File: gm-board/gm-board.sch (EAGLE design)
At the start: 43 parts, among them IC1 ZXCT1109, J1 SWD_SHROUD, J2 HV_GEN

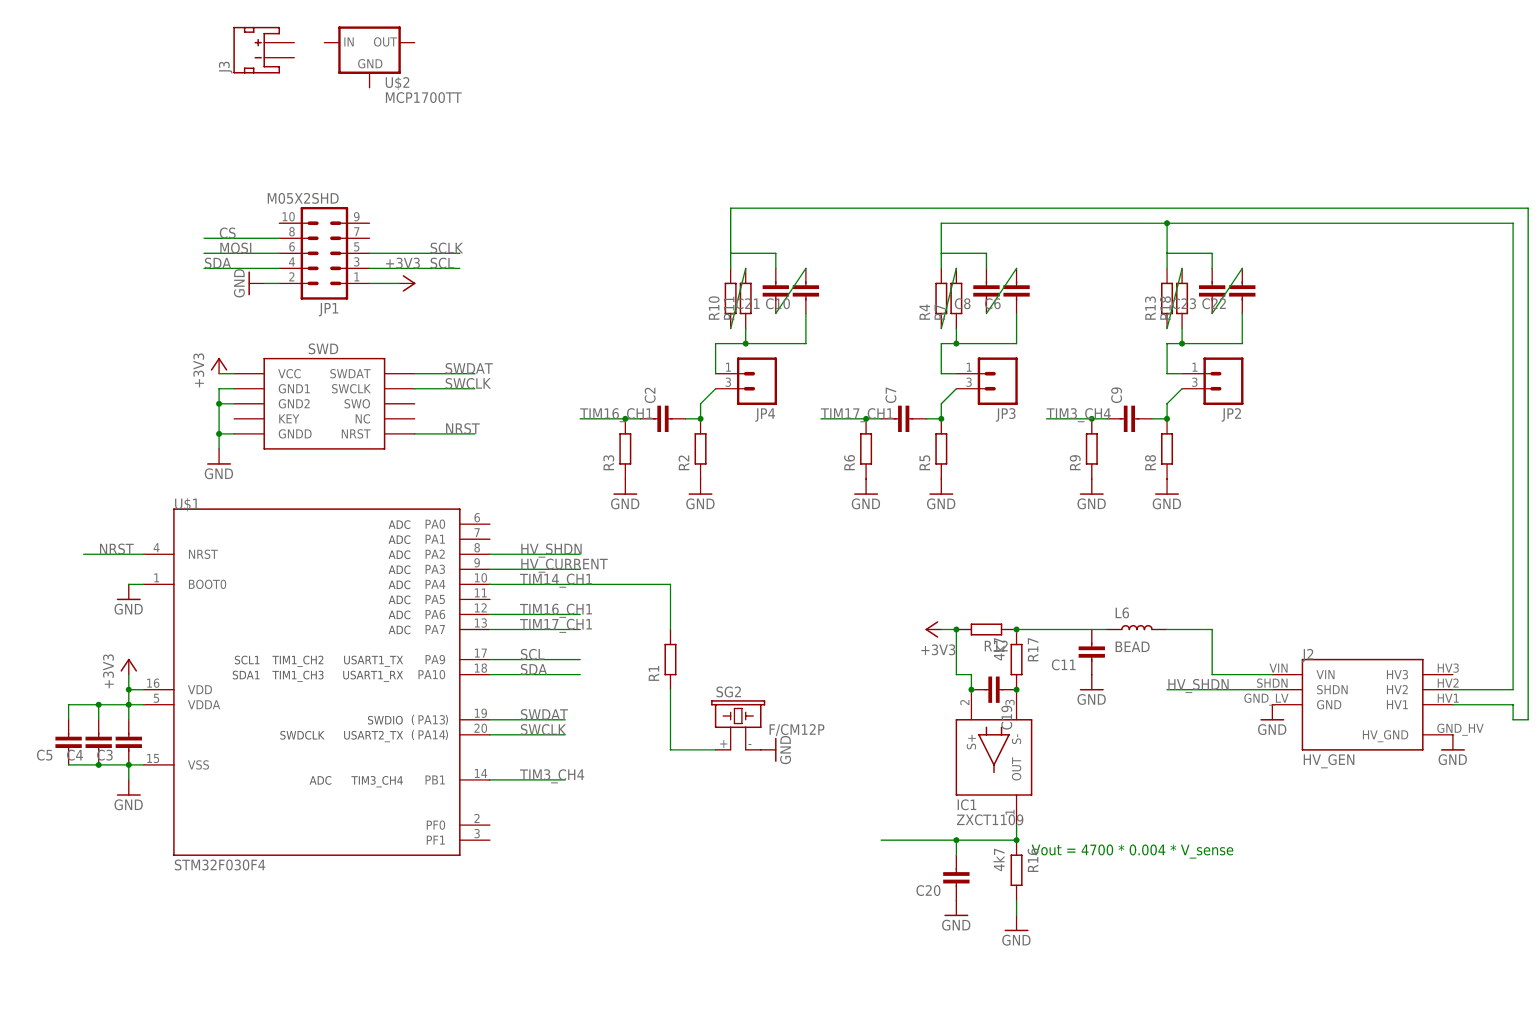
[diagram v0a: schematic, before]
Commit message: adding part ordering numbers
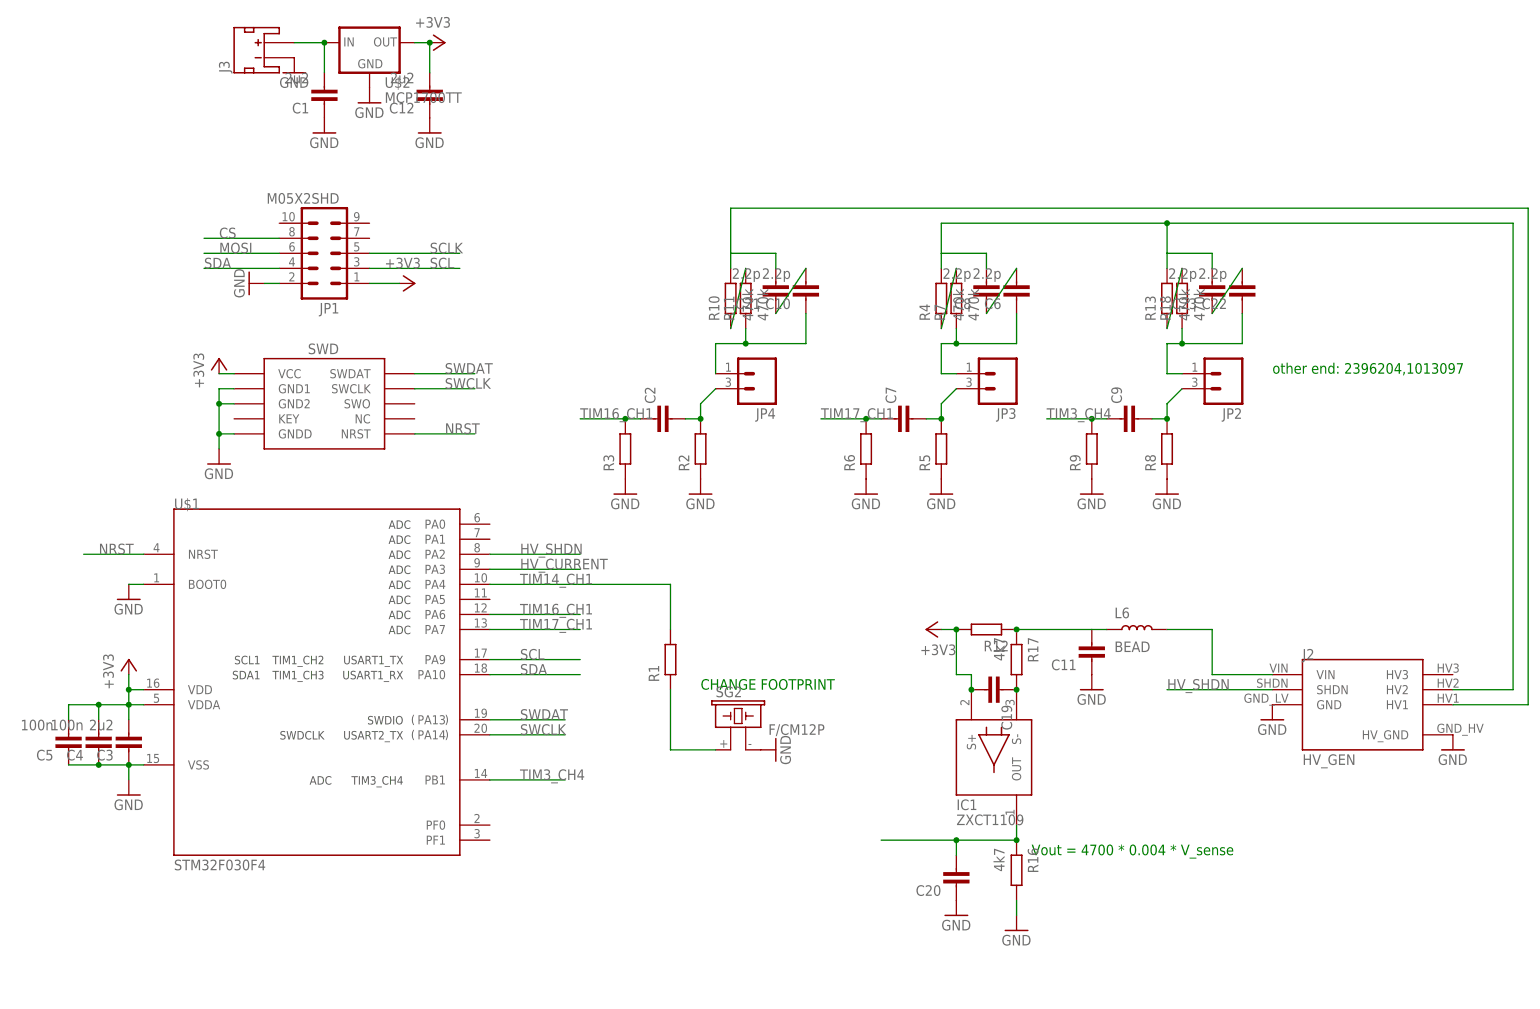
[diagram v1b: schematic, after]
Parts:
- added C1, C12: 2u2, passives-7351:CAPACITOR0603-N
- C10, C21, C22, C23, C6, C8: value (none) -> 2.2p; FARNELL (none) -> 1855767
- C3: value (none) -> 2u2; FARNELL (none) -> 2496923
- C4, C5: value (none) -> 100n
- IC1: FARNELL (none) -> 1904028
- JP2, JP3, JP4: FARNELL (none) -> 1462950
- L6: FARNELL (none) -> 1781093
- R10, R13, R18, R4, R7: value (none) -> 470k; FARNELL (none) -> 1576201
- R11: value (none) -> 470k
- R12: FARNELL (none) -> 2328089
- SG2: FARNELL (none) -> 1823866
- U$1: FARNELL (none) -> 2393635
- U$2: FANRELL (none) -> 1296592
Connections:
- new net N$10: C1.2, J3.+, U$2.IN
- net +3V3: now also C12.2, U$2.OUT
- net GND: now also C1.1, C12.1, J3.-, U$2.GND
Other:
- note added: "CHANGE FOOTPRINT"
- note added: "other end: 2396204,1013097"

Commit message: almost done
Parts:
- removed C19: (no value), passives-7351:CAPACITOR0603-N
- removed C22, C23: 2.2p, passives-7351:CAPACITOR0805-N
- removed R17: 4k7, passives-7351:RESISTOR0603-N
- removed R18: 470k, passives-7351:RESISTOR1206-N
- removed SG2: F/CM12P, buzzer:F/CM12P
- removed U$2: MCP1700TT, dtb:MCP1700TT
- added C13: (no value), passives-7351:CAPACITOR0603-N
- added C16: 2.2p, passives-7351:CAPACITOR0805-N
- added C17: 100n, passives-7351:CAPACITOR0603-N
- added IC2: ZXCT1109, dtb:ZXCT1109
- added R14, R15: 470k, passives-7351:RESISTOR1206-N
- added SJ1: JUMPER-PAD-3-2OF3_NC_BY_PASTE, SparkFun-Passives:JUMPER-PAD-3-2OF3_NC_BY_PASTE
- added X1: PKM13EPYH, Mine:PKM13EPYH
- C1, C12, C3: value 2u2 -> (none); FARNELL 2496923 -> (none)
- C11: value (none) -> 2.2p; device passives-7351:CAPACITOR0603-N -> passives-7351:CAPACITOR0805-N; FARNELL (none) -> 1855767
- C2, C9: value (none) -> 2u2; FARNELL (none) -> 2496923
- C4: value 100n -> 2u2; FARNELL (none) -> 2496923
- C5: value 100n -> 2.2p; device passives-7351:CAPACITOR0603-N -> passives-7351:CAPACITOR0805-N; FARNELL (none) -> 1855767
- C8: value 2.2p -> 100n; device passives-7351:CAPACITOR0805-N -> passives-7351:CAPACITOR0603-N; FARNELL 1855767 -> (none)
- IC1: value ZXCT1109 -> MCP1700TT; device dtb:ZXCT1109 -> dtb:MCP1700TT; FANRELL (none) -> 1296592; FARNELL 1904028 -> (none)
- J1: value SWD_SHROUD -> HV_GEN-HOLE; device dtb:SWD_SHROUD -> generator-lib:HV_GEN-HOLE
- J2: value HV_GEN -> (none); device generator-lib:HV_GEN -> dtb:JST_2MM_MALE_TH
- J3: value (none) -> SWD_SHROUD; device dtb:JST_2MM_MALE_TH -> dtb:SWD_SHROUD
- JP1: value M05X2SHD -> (none); device SparkFun-Connectors:M05X2SHD -> Mine:M02-HV; FARNELL (none) -> 1462950
- JP2: value (none) -> M05X2SHD; device Mine:M02-HV -> SparkFun-Connectors:M05X2SHD; FARNELL 1462950 -> (none)
- R1, R6: value (none) -> 4k7
- R11: value 470k -> (none); device passives-7351:RESISTOR1206-N -> passives-7351:RESISTOR0603-N
- R12: FARNELL 2328089 -> (none)
- R13, R7: value 470k -> (none); device passives-7351:RESISTOR1206-N -> passives-7351:RESISTOR0603-N; FARNELL 1576201 -> (none)
- R16: value 4k7 -> (none)
- R2: FARNELL (none) -> 2328089
- R3, R9: value (none) -> 470k; device passives-7351:RESISTOR0603-N -> passives-7351:RESISTOR1206-N; FARNELL (none) -> 1576201
- renumbered C20 to C14, C21 to C15, L6 to L1, U$1 to IC3
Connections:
- removed net N$10: C1.2, J3.+, U$2.IN
- new net N$11: C3.2, IC2.S+, R2.P$2, SJ1.2
- new net VIN: C4.2, IC1.IN, J2.+, SJ1.1
- net +3V3: now also C17.2, C2.2, C8.2, C9.2, IC1.OUT, J3.VCC, JP2.1, SJ1.3; no longer C12.2, C19.2, C3.2, C4.2, C5.2, IC1.S+, J1.VCC, JP1.1, R12.P$2, U$2.OUT
- net CS: now also JP2.8; no longer JP1.8
- net GND: now also C17.1, C2.1, C8.1, C9.1, IC1.GND, J1.GND, J1.HV_GND, J2.-, J3.GND1, J3.GND2, J3.GNDD, JP2.2, R11.P$1, R13.P$1, R16.P$1, R6.P$2, R7.P$1, X1.2; no longer C11.1, C12.1, C3.1, C5.1, J1.GND1, J1.GND2, J1.GNDD, J2.GND, J2.HV_GND, J3.-, JP1.2, R16.P$2, R2.P$1, R3.P$1, R6.P$1, R9.P$1, SG2.2, U$2.GND
- net HV_CURRENT: now also IC2.OUT, R6.P$1; no longer IC1.OUT, R16.P$1
- net HV_SHDN: now also J1.SHDN; no longer J2.SHDN
- net MOSI: now also JP2.6; no longer JP1.6
- net N$1: now also C13.2, R13.P$2; no longer C2.2, R2.P$2
- net N$16: now also C16.2; no longer C10.2
- net N$18: now also C3.1, IC2.S-, R1.P$2; no longer C19.1, IC1.S-, R17.P$2
- net N$19: now also C11.1, R10.P$1; no longer C6.1, R7.P$1
- net N$2: now also J1.VIN; no longer J2.VIN
- net N$20: now also C10.2, C5.2, J1.HV2, R3.P$2, R9.P$2; no longer C23.2, C8.2, J2.HV2, R13.P$2, R4.P$2
- net N$21: now also R10.P$2, R9.P$1; no longer R4.P$1, R7.P$2
- net N$22: now also C10.1, C11.2; no longer C6.2, C8.1
- net N$23: now also C6.1, JP1.1, R4.P$1; no longer C22.1, JP2.1, R18.P$1
- net N$25: now also R3.P$1, R4.P$2; no longer R13.P$1, R18.P$2
- net N$26: now also C5.1, C6.2; no longer C22.2, C23.1
- net N$3: now also C16.1, R15.P$1; no longer C10.1, R11.P$1
- net N$4: now also R14.P$1, R15.P$2; no longer R10.P$1, R11.P$2
- net N$5: now also C12.2, R11.P$2; no longer C7.2, R5.P$2
- net N$6: now also R12.P$1, X1.1; no longer R1.P$1, SG2.1
- net N$7: now also C1.2, R1.P$1, R2.P$1; no longer C11.2, R12.P$1, R17.P$1
- net N$8: now also J1.HV1, R14.P$2; no longer J2.HV1, R10.P$2
- net N$9: now also C7.2, JP1.2, R5.P$2; no longer C9.2, JP2.2, R8.P$2
- net NRST: now also J3.NRST; no longer J1.NRST
- net SCL: now also JP2.3; no longer JP1.3
- net SCLK: now also JP2.5; no longer JP1.5
- net SDA: now also JP2.4; no longer JP1.4
- net SWCLK: now also J3.SWCLK; no longer J1.SWCLK
- net SWDAT: now also J3.SWDAT; no longer J1.SWDAT
- net TIM14_CH1: now also R12.P$2; no longer R1.P$2
- net TIM16_CH1: now also C13.1, R16.P$2; no longer C2.1, R3.P$2
- net TIM17_CH1: now also C12.1, R8.P$2; no longer C7.1, R6.P$2
- net TIM3_CH4: now also C7.1, R7.P$2; no longer C9.1, R9.P$2
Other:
- note removed: "CHANGE FOOTPRINT"
- moved on the sheet: C1, C10, C11, C12, C2, C3, C4, C5, C6, C7, C8, C9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

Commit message: gettuing there...
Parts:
- added R17, R18: (no value), passives-7351:RESISTOR0603-N
- added TP1, TP2, TP3, TP4, TP5, TP6: TPTP09R, testpad:TPTP09R
- added X2: GM-TUBE, Mine:GM-TUBE
- J2: device dtb:JST_2MM_MALE_TH -> dtb:JST_2MM_MALE_TH-NT
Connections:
- new net N$10: J1.HV3, TP1.TP
- new net N$12: J1.HV2, TP2.TP, TP6.TP
- new net N$13: J1.HV1, TP3.TP
- net +3V3: now also R17.P$2, R18.P$2
- net N$1: now also X2.-
- net N$20: now also TP4.TP; no longer J1.HV2
- net N$3: now also X2.+
- net N$8: now also TP5.TP; no longer J1.HV1
- net SCL: now also R17.P$1
- net SDA: now also R18.P$1
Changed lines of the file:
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@@
 <?xml version="1.0" encoding="utf-8"?>
 <!DOCTYPE eagle SYSTEM "eagle.dtd">
-<eagle version="6.5.0">
+<eagle version="6.6.0">
 <drawing>
 <settings>
@@
 <part name="J1" library="generator-lib" deviceset="HV_GEN" device="-HOLE" value="HV_GEN-HOLE"/>
 <part name="GND25" library="supply1" deviceset="GND" device=""/>
-<part name="J2" library="dtb" deviceset="JST_2MM_MALE_TH" device=""/>
+<part name="J2" library="dtb" deviceset="JST_2MM_MALE_TH" device="-NT"/>
 <part name="IC1" library="dtb" deviceset="MCP1700" device="TT">
 <attribute name="FANRELL" value="1296592"/>
@@
 <part name="SJ1" library="SparkFun-Passives" deviceset="JUMPER-PAD-3-2OF3_NC_BY_PASTE" device=""/>
 <part name="+3V4" library="supply1" deviceset="+3V3" device=""/>
+<part name="X2" library="Mine" deviceset="GM-TUBE" device=""/>
+<part name="TP3" library="testpad" deviceset="TP" device="TP09R"/>
+<part name="TP1" library="testpad" deviceset="TP" device="TP09R"/>
+<part name="TP2" library="testpad" deviceset="TP" device="TP09R"/>
+<part name="TP4" library="testpad" deviceset="TP" device="TP09R"/>
+<part name="TP5" library="testpad" deviceset="TP" device="TP09R"/>
+<part name="TP6" library="testpad" deviceset="TP" device="TP09R"/>
+<part name="R17" library="passives-7351" deviceset="RESISTOR" device="0603-N"/>
+<part name="R18" library="passives-7351" deviceset="RESISTOR" device="0603-N"/>
+<part name="+3V5" library="supply1" deviceset="+3V3" device=""/>
+<part name="+3V7" library="supply1" deviceset="+3V3" device=""/>
 </parts>
 <sheets>
@@
 <instance part="SJ1" gate="G$1" x="144.78" y="50.8" rot="R180"/>
 <instance part="+3V4" gate="G$1" x="144.78" y="58.42"/>
+<instance part="X2" gate="G$1" x="104.14" y="101.6"/>
+<instance part="TP3" gate="G$1" x="238.76" y="38.1" rot="R270"/>
+<instance part="TP1" gate="G$1" x="238.76" y="43.18" rot="R270"/>
+<instance part="TP2" gate="G$1" x="238.76" y="40.64" rot="R270"/>
+<instance part="TP4" gate="G$1" x="243.84" y="40.64" rot="R90"/>
+<instance part="TP5" gate="G$1" x="246.38" y="38.1" rot="R90"/>
+<instance part="TP6" gate="G$1" x="238.76" y="40.64" rot="R270"/>
+<instance part="R17" gate="G$1" x="76.2" y="124.46" rot="R90"/>
+<instance part="R18" gate="G$1" x="20.32" y="121.92" rot="R90"/>
+<instance part="+3V5" gate="G$1" x="76.2" y="132.08"/>
+<instance part="+3V7" gate="G$1" x="20.32" y="129.54"/>
 </instances>
 <busses>
@@
 <junction x="109.22" y="86.36"/>
 <pinref part="JP4" gate="G$1" pin="2"/>
+<pinref part="X2" gate="G$1" pin="-"/>
+<wire x1="101.6" y1="93.98" x2="109.22" y2="93.98" width="0.1524" layer="91"/>
+<wire x1="109.22" y1="93.98" x2="109.22" y2="88.9" width="0.1524" layer="91"/>
 </segment>
 </net>
@@
 <junction x="116.84" y="99.06"/>
 <pinref part="JP4" gate="G$1" pin="1"/>
+<pinref part="X2" gate="G$1" pin="+"/>
+<wire x1="104.14" y1="114.3" x2="111.76" y2="114.3" width="0.1524" layer="91"/>
+<wire x1="111.76" y1="114.3" x2="111.76" y2="99.06" width="0.1524" layer="91"/>
 </segment>
 </net>
@@
 <wire x1="114.3" y1="121.92" x2="248.92" y2="121.92" width="0.1524" layer="91"/>
 <wire x1="248.92" y1="121.92" x2="248.92" y2="38.1" width="0.1524" layer="91"/>
-<pinref part="J1" gate="G$1" pin="HV1"/>
-<wire x1="248.92" y1="38.1" x2="236.22" y2="38.1" width="0.1524" layer="91"/>
+<pinref part="TP5" gate="G$1" pin="TP"/>
 </segment>
 </net>
@@
 <pinref part="+3V4" gate="G$1" pin="+3V3"/>
 </segment>
+<segment>
+<pinref part="R17" gate="G$1" pin="P$2"/>
+<pinref part="+3V5" gate="G$1" pin="+3V3"/>
+</segment>
+<segment>
+<pinref part="R18" gate="G$1" pin="P$2"/>
+<pinref part="+3V7" gate="G$1" pin="+3V3"/>
+</segment>
 </net>
 <net name="SCL" class="0">
@@
 <segment>
 <pinref part="JP2" gate="G$1" pin="3"/>
-<wire x1="53.34" y1="111.76" x2="68.58" y2="111.76" width="0.1524" layer="91"/>
 <label x="63.5" y="111.76" size="1.778" layer="95"/>
+<wire x1="53.34" y1="111.76" x2="76.2" y2="111.76" width="0.1524" layer="91"/>
+<pinref part="R17" gate="G$1" pin="P$1"/>
+<wire x1="76.2" y1="111.76" x2="83.82" y2="111.76" width="0.1524" layer="91"/>
+<wire x1="76.2" y1="119.38" x2="76.2" y2="111.76" width="0.1524" layer="91"/>
+<junction x="76.2" y="111.76"/>
 </segment>
 </net>
@@
 <segment>
 <pinref part="JP2" gate="G$1" pin="4"/>
-<wire x1="38.1" y1="111.76" x2="25.4" y2="111.76" width="0.1524" layer="91"/>
 <label x="25.4" y="111.76" size="1.778" layer="95"/>
+<wire x1="38.1" y1="111.76" x2="20.32" y2="111.76" width="0.1524" layer="91"/>
+<pinref part="R18" gate="G$1" pin="P$1"/>
+<wire x1="20.32" y1="111.76" x2="12.7" y2="111.76" width="0.1524" layer="91"/>
+<wire x1="20.32" y1="116.84" x2="20.32" y2="111.76" width="0.1524" layer="91"/>
+<junction x="20.32" y="111.76"/>
 </segment>
 </net>
@@
 <wire x1="187.96" y1="119.38" x2="246.38" y2="119.38" width="0.1524" layer="91"/>
 <wire x1="246.38" y1="119.38" x2="246.38" y2="40.64" width="0.1524" layer="91"/>
-<pinref part="J1" gate="G$1" pin="HV2"/>
-<wire x1="246.38" y1="40.64" x2="236.22" y2="40.64" width="0.1524" layer="91"/>
 <pinref part="R3" gate="G$1" pin="P$2"/>
 <wire x1="187.96" y1="111.76" x2="187.96" y2="114.3" width="0.1524" layer="91"/>
@@
 <wire x1="195.58" y1="114.3" x2="195.58" y2="111.76" width="0.1524" layer="91"/>
 <junction x="187.96" y="119.38"/>
+<pinref part="TP4" gate="G$1" pin="TP"/>
 </segment>
 </net>
@@
 </segment>
 </net>
+<net name="N$10" class="0">
+<segment>
+<pinref part="J1" gate="G$1" pin="HV3"/>
+<pinref part="TP1" gate="G$1" pin="TP"/>
+</segment>
+</net>
+<net name="N$12" class="0">
+<segment>
+<pinref part="J1" gate="G$1" pin="HV2"/>
+<pinref part="TP2" gate="G$1" pin="TP"/>
+<pinref part="TP6" gate="G$1" pin="TP"/>
+<junction x="236.22" y="40.64"/>
+<pinref part="TP6" gate="G$1" pin="TP"/>
+</segment>
+</net>
+<net name="N$13" class="0">
+<segment>
+<pinref part="J1" gate="G$1" pin="HV1"/>
+<pinref part="TP3" gate="G$1" pin="TP"/>
+</segment>
+</net>
